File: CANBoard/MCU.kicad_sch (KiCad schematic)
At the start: 23 parts

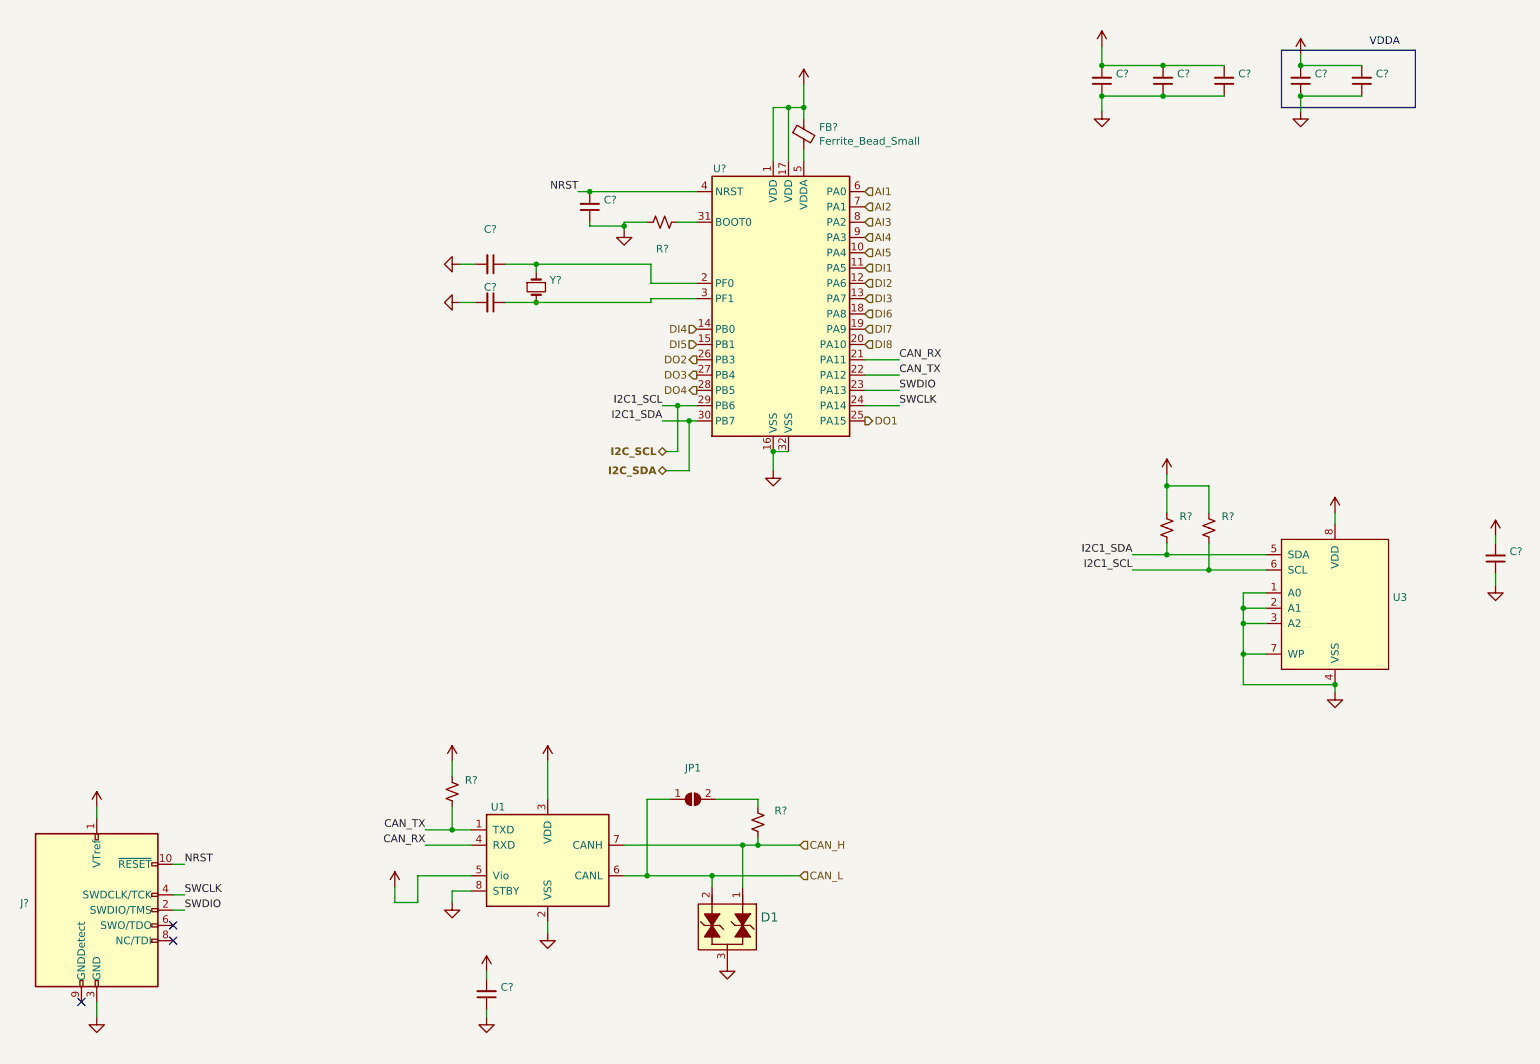
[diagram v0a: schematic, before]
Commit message: V2 updates
Removed FRAM, I2C and SWD pins. Added ID solder jumpers and Tag Connect
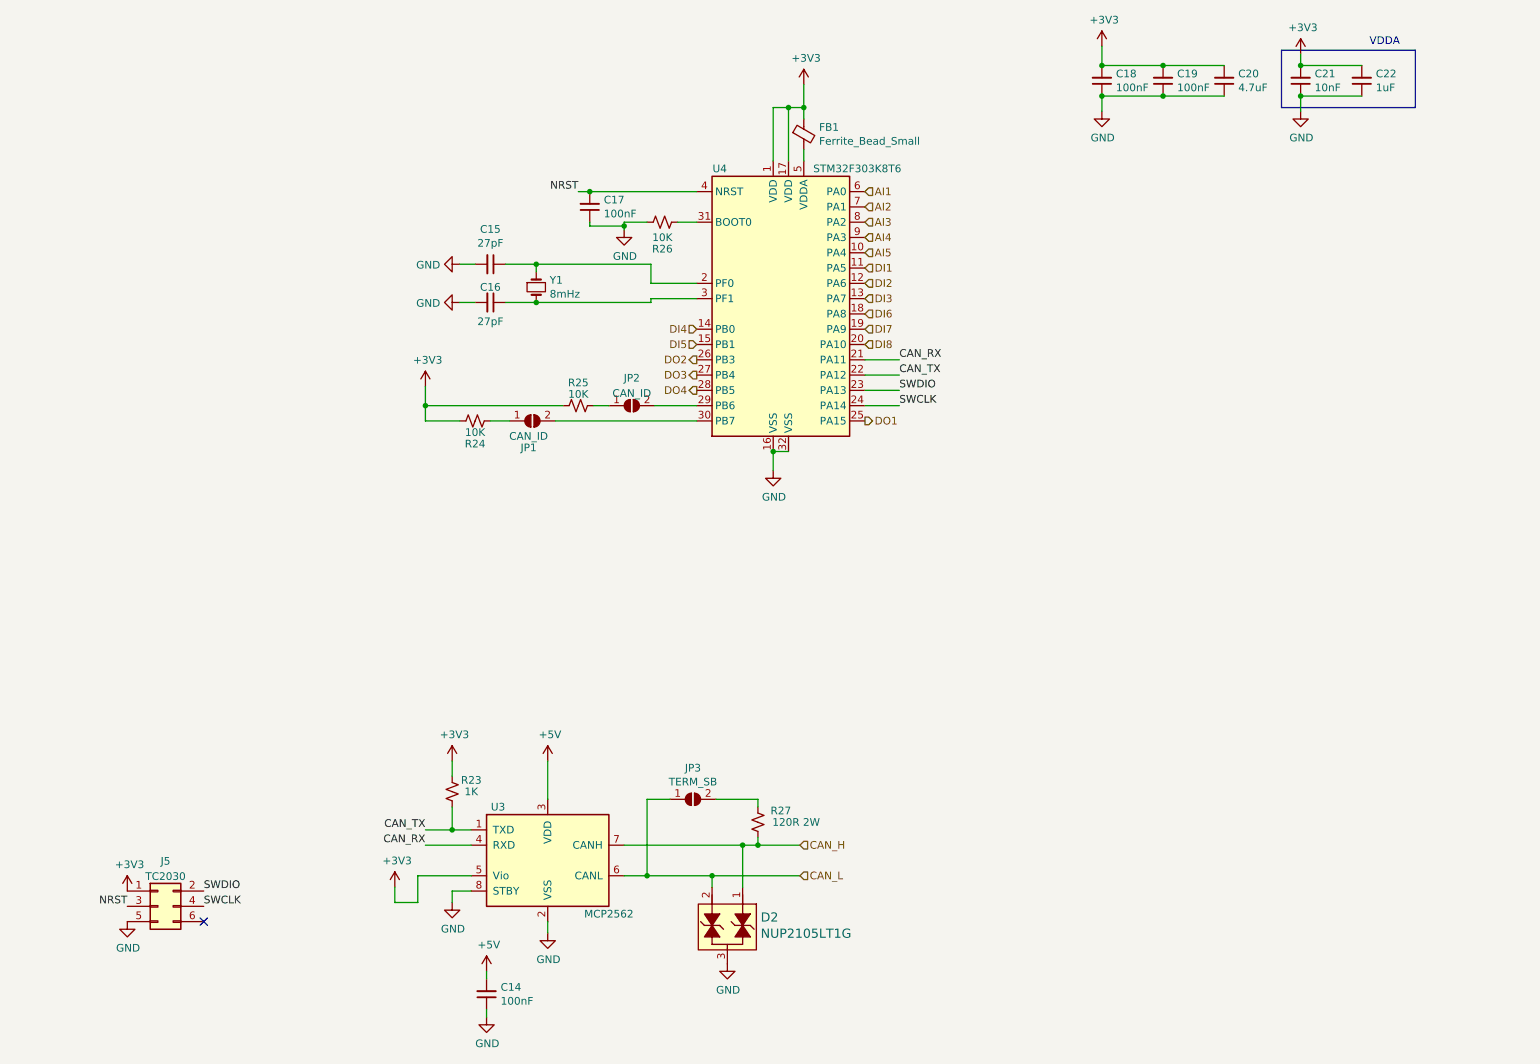
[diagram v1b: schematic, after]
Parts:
- removed C?: (no value), symbol Device:C_Small
- removed J?: (no value), symbol Connector:Conn_ARM_JTAG_SWD_10
- removed U3: (no value), symbol Memory_FRAM:MB85RC256V
- added J5: TC2030, Connector:Tag-Connect_TC2030-IDC-NL_2x03_P1.27mm_Vertical, symbol Connector_Generic:Conn_02x03_Odd_Even
- added JP1, JP2: CAN_ID, Jumper:SolderJumper-2_P1.3mm_Open_RoundedPad1.0x1.5mm, symbol Jumper:SolderJumper_2_Open
- C14, C17, C18, C19: renamed from C?; value (none) -> 100nF; footprint (none) -> Capacitor_SMD:C_0805_2012Metric
- C15, C16: renamed from C?; value (none) -> 27pF; footprint (none) -> Capacitor_SMD:C_0805_2012Metric
- C20: renamed from C?; value (none) -> 4.7uF; footprint (none) -> Capacitor_SMD:C_0805_2012Metric
- C21: renamed from C?; value (none) -> 10nF; footprint (none) -> Capacitor_SMD:C_0805_2012Metric
- C22: renamed from C?; value (none) -> 1uF; footprint (none) -> Capacitor_SMD:C_0805_2012Metric
- D2: renamed from D1; value (none) -> NUP2105LT1G; footprint (none) -> digikey-footprints:SOT-23-3
- JP3: renamed from JP1; value (none) -> TERM_SB; footprint (none) -> Jumper:SolderJumper-2_P1.3mm_Open_RoundedPad1.0x1.5mm
- R23: renamed from R?; value (none) -> 1K; footprint (none) -> Resistor_SMD:R_0805_2012Metric
- R24, R25, R26: renamed from R?; value (none) -> 10K; footprint (none) -> Resistor_SMD:R_0805_2012Metric
- R27: renamed from R?; value (none) -> 120R 2W; footprint (none) -> Resistor_SMD:R_2512_6332Metric
- U3: renamed from U1; value (none) -> MCP2562; footprint (none) -> Package_SO:SOIC-8_3.9x4.9mm_P1.27mm
- U4: renamed from U?; value (none) -> STM32F303K8T6; footprint (none) -> Package_QFP:LQFP-32_7x7mm_P0.8mm
- Y1: renamed from Y?; value (none) -> 8mHz; footprint (none) -> Crystal:Crystal_SMD_5032-2Pin_5.0x3.2mm
- gave numbers to parts that had none: 1
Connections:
- net +3V3: now also J5.1 (Pin_1)
- net GND: now also J5.5 (Pin_5)
- net NRST: now also J5.3 (Pin_3)
- net SWCLK: now also J5.4 (Pin_4)
- net SWDIO: now also J5.2 (Pin_2)
- net I2C_SCL: no longer names the net of U4.29 (PB6)
- net I2C_SCL: now also JP2.2 (B); no longer R24.1
- net I2C_SDA: no longer names the net of U4.30 (PB7)
- net I2C_SDA: now also JP1.2 (B); no longer R25.1
- new net: JP2.1 (A), R25.1
- new net: JP1.1 (A), R24.1
- no-connect marks 3 -> 1
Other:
- moved on the sheet: R24, R25

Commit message: Updated outputs, added JLCPCB LCSC part nums
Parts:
- C14, C17, C18, C19: LCSC (none) -> C49678
- C15, C16: LCSC (none) -> C1808
- C20: LCSC (none) -> C1779
- C21: LCSC (none) -> C1710
- C22: LCSC (none) -> C28323
- D2: LCSC (none) -> C2890118
- FB1: LCSC (none) -> C85840
- R23: LCSC (none) -> C17513
- R24, R25, R26: LCSC (none) -> C17414
- R27: LCSC (none) -> C19865
- U3: Digi-Key_PN (none) -> MCP2562-H/SN-ND; LCSC (none) -> C191417
- U4: Digi-Key_PN 497-13318-ND -> 497-15828-ND; LCSC (none) -> C118318
- Y1: LCSC (none) -> C144380
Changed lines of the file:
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@@
       (effects (font (size 1.27 1.27)) hide)
     )
-    (property "Digi-Key_PN" "497-13318-ND" (at 149.225 71.755 0)
+    (property "Digi-Key_PN" "497-15828-ND" (at 149.225 71.755 0)
+      (effects (font (size 1.27 1.27)) hide)
+    )
+    (property "LCSC" "C118318" (at 149.225 71.755 0)
       (effects (font (size 1.27 1.27)) hide)
     )
@@
       (effects (font (size 1.27 1.27)) hide)
     )
+    (property "LCSC" "C144380" (at 107.315 69.85 0)
+      (effects (font (size 1.27 1.27)) hide)
+    )
     (pin "1")
     (pin "2")
@@
       (effects (font (size 1.27 1.27)) hide)
     )
+    (property "LCSC" "C1808" (at 99.695 66.04 0)
+      (effects (font (size 1.27 1.27)) hide)
+    )
     (pin "1")
     (pin "2")
@@
       (effects (font (size 1.27 1.27)) hide)
     )
+    (property "LCSC" "C1808" (at 99.695 72.39 0)
+      (effects (font (size 1.27 1.27)) hide)
+    )
     (pin "1")
     (pin "2")
@@
     )
     (property "Digi-Key_PN" "311-10.0KCRDKR-ND" (at 128.27 59.055 0)
+      (effects (font (size 1.27 1.27)) hide)
+    )
+    (property "LCSC" "C17414" (at 128.27 59.055 0)
       (effects (font (size 1.27 1.27)) hide)
     )
@@
       (effects (font (size 1.27 1.27)) hide)
     )
+    (property "LCSC" "C85840" (at 151.765 44.45 0)
+      (effects (font (size 1.27 1.27)) hide)
+    )
     (pin "1")
     (pin "2")
@@
       (effects (font (size 1.27 1.27)) hide)
     )
+    (property "LCSC" "C49678" (at 116.205 56.515 0)
+      (effects (font (size 1.27 1.27)) hide)
+    )
     (pin "1")
     (pin "2")
@@
       (effects (font (size 1.27 1.27)) hide)
     )
+    (property "LCSC" "C49678" (at 201.295 35.56 0)
+      (effects (font (size 1.27 1.27)) hide)
+    )
     (pin "1")
     (pin "2")
@@
       (effects (font (size 1.27 1.27)) hide)
     )
+    (property "LCSC" "C49678" (at 211.455 35.56 0)
+      (effects (font (size 1.27 1.27)) hide)
+    )
     (pin "1")
     (pin "2")
@@
       (effects (font (size 1.27 1.27)) hide)
     )
+    (property "LCSC" "C1779" (at 221.615 35.56 0)
+      (effects (font (size 1.27 1.27)) hide)
+    )
     (pin "1")
     (pin "2")
@@
       (effects (font (size 1.27 1.27)) hide)
     )
+    (property "LCSC" "C1710" (at 234.315 35.56 0)
+      (effects (font (size 1.27 1.27)) hide)
+    )
     (pin "1")
     (pin "2")
@@
       (effects (font (size 1.27 1.27)) hide)
     )
+    (property "LCSC" "C28323" (at 244.475 35.56 0)
+      (effects (font (size 1.27 1.27)) hide)
+    )
     (pin "1")
     (pin "2")
@@
     )
     (property "Digi-Key_PN" "311-1.0KARCT-ND" (at 93.345 153.67 0)
+      (effects (font (size 1.27 1.27)) hide)
+    )
+    (property "LCSC" "C17513" (at 93.345 153.67 0)
       (effects (font (size 1.27 1.27)) hide)
     )
@@
       (effects (font (size 1.524 1.524)) (justify left) hide)
     )
+    (property "LCSC" "C2890118" (at 139.065 177.165 0)
+      (effects (font (size 1.27 1.27)) hide)
+    )
     (pin "1")
     (pin "2")
@@
       (effects (font (size 1.27 1.27)) hide)
     )
+    (property "LCSC" "" (at 133.35 154.94 0)
+      (effects (font (size 1.27 1.27)) hide)
+    )
     (pin "1")
     (pin "2")
@@
       (effects (font (size 1.27 1.27)) hide)
     )
+    (property "LCSC" "C19865" (at 144.145 158.75 0)
+      (effects (font (size 1.27 1.27)) hide)
+    )
     (pin "1")
     (pin "2")
@@
       (effects (font (size 1.27 1.27)) hide)
     )
+    (property "LCSC" "C49678" (at 99.06 187.325 0)
+      (effects (font (size 1.27 1.27)) hide)
+    )
     (pin "1")
     (pin "2")
@@
       (effects (font (size 1.27 1.27)) hide)
     )
+    (property "LCSC" "C17414" (at 114.3 89.535 0)
+      (effects (font (size 1.27 1.27)) hide)
+    )
     (pin "1")
     (pin "2")
@@
     )
     (property "Digi-Key_PN" "311-10.0KCRDKR-ND" (at 97.155 92.075 0)
+      (effects (font (size 1.27 1.27)) hide)
+    )
+    (property "LCSC" "C17414" (at 97.155 92.075 0)
       (effects (font (size 1.27 1.27)) hide)
     )
@@
     )
     (property "Datasheet" "http://ww1.microchip.com/downloads/en/DeviceDoc/25167A.pdf" (at 109.22 165.1 0)
+      (effects (font (size 1.27 1.27)) hide)
+    )
+    (property "Digi-Key_PN" "MCP2562-H/SN-ND" (at 109.22 165.1 0)
+      (effects (font (size 1.27 1.27)) hide)
+    )
+    (property "LCSC" "C191417" (at 109.22 165.1 0)
       (effects (font (size 1.27 1.27)) hide)
     )
@@
       (effects (font (size 1.27 1.27)) hide)
     )
+    (property "LCSC" "" (at 44.45 172.72 0)
+      (effects (font (size 1.27 1.27)) hide)
+    )
     (pin "1")
     (pin "2")
@@
       (effects (font (size 1.27 1.27)) hide)
     )
+    (property "LCSC" "" (at 123.19 89.535 0)
+      (effects (font (size 1.27 1.27)) hide)
+    )
     (pin "1")
     (pin "2")
@@
       (effects (font (size 1.27 1.27)) hide)
     )
+    (property "LCSC" "" (at 106.68 92.075 0)
+      (effects (font (size 1.27 1.27)) hide)
+    )
